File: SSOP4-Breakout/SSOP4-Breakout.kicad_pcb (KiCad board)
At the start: 2 copper layers, 13.8 x 13.8 mm, 3 parts, among them J1 Conn_01x05_Male, J2 Conn_01x05_Male, U1 SSOP-8-I

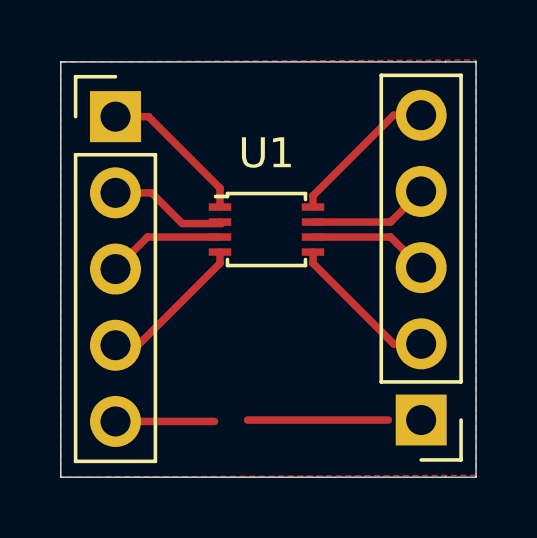
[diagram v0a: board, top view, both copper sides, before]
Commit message: get the SSOP4 breakout designed
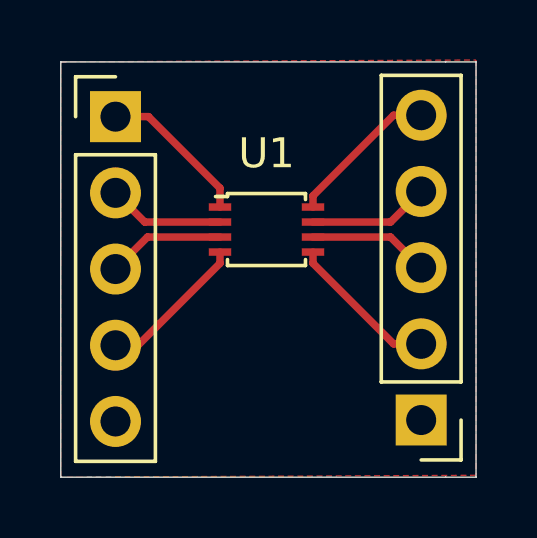
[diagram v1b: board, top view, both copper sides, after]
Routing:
- net GND: track 8.00 -> 0.00 mm
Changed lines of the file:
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@@
-(kicad_pcb (version 20171130) (host pcbnew 5.1.5+dfsg1-2build2)
+(kicad_pcb (version 20171130) (host pcbnew "(5.1.5-0-10_14)")
   (general
     (thickness 1.6)
     (drawings 6)
-    (tracks 26)
+    (tracks 22)
     (zones 0)
     (modules 3)
@@
     (visible_elements FFFFFF7F)
     (pcbplotparams
-      (layerselection 0x010fc_ffffffff)
+      (layerselection 0x290aa_7fffffff)
       (usegerberextensions false)
       (usegerberattributes false)
       (usegerberadvancedattributes false)
       (creategerberjobfile false)
-      (excludeedgelayer true)
+      (excludeedgelayer false)
       (linewidth 0.100000)
       (plotframeref false)
@@
       (plotvalue true)
       (plotinvisibletext false)
-      (padsonsilk false)
+      (padsonsilk true)
       (subtractmaskfromsilk false)
       (outputformat 1)
       (mirror false)
-      (drillshape 1)
+      (drillshape 0)
       (scaleselection 1)
       (outputdirectory ""))
@@
   (segment (start 14.957002 17.903) (end 17.373 17.903) (width 0.25) (layer F.Cu) (net 2))
   (segment (start 13.890001 18.970001) (end 14.957002 17.903) (width 0.25) (layer F.Cu) (net 2))
-  (segment (start 17.422999 17.452999) (end 17.373 17.403) (width 0.25) (layer F.Cu) (net 3))
-  (segment (start 13.890001 16.430001) (end 15.092082 16.430001) (width 0.25) (layer F.Cu) (net 3))
-  (segment (start 16.11508 17.452999) (end 17.422999 17.452999) (width 0.25) (layer F.Cu) (net 3))
-  (segment (start 15.092082 16.430001) (end 16.11508 17.452999) (width 0.25) (layer F.Cu) (net 3))
+  (segment (start 14.863 17.403) (end 13.890001 16.430001) (width 0.25) (layer F.Cu) (net 3))
+  (segment (start 17.373 17.403) (end 14.863 17.403) (width 0.25) (layer F.Cu) (net 3))
   (segment (start 17.373 16.273) (end 17.373 16.528) (width 0.25) (layer F.Cu) (net 4))
   (segment (start 14.990001 13.890001) (end 17.373 16.273) (width 0.25) (layer F.Cu) (net 4))
@@
   (segment (start 20.473 18.778) (end 23.158 21.463) (width 0.25) (layer F.Cu) (net 8))
   (segment (start 20.473 18.403) (end 20.473 18.778) (width 0.25) (layer F.Cu) (net 8))
-  (segment (start 13.890001 24.050001) (end 17.192001 24.050001) (width 0.25) (layer F.Cu) (net 9))
-  (segment (start 22.987 24.003) (end 18.288 24.003) (width 0.25) (layer F.Cu) (net 9))
   (zone (net 9) (net_name GND) (layer F.Cu) (hatch edge 0.508)
     (connect_pads (clearance 0.508))
